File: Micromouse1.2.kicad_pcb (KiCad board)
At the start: 2 copper layers, 70.4 x 87.9 mm, 132 parts, among them J1 USB_B, P1 CONN_01X4, Q1 Q_NMOS_DGS, Q2 Q_NMOS_DGS, Q3 Q_NMOS_DGS, Q4 Q_NMOS_DGS, Q5 Q_NMOS_DGS, Q6 Q_NMOS_DGS, U1 BAT54C, U10 CONN_02X03, U14 600, U15 LMZ21701, U16 JST_Connector, U17 Switch_micromouse, U18 LMZ21701, U19 splitter, U2 DRV8833, U20 TPD3S014, U21 MKL02Z32VFG4, U22 LP38691, U23 MK66FX1M0, U24 Test_Point, U25 Test_Point, U26 Test_Point, U27 Test_Point, U28 Test_Point, U29 Test_Point, U3 120, U30 Test_Point, U31 MPU-6500, U32 Motor_mount, U4 TPS61222DCK, U5 600, U6 BAT54C, U7 Test_Point, U9 CONN_02X03, Y1 Crystal_16MHz, Y2 32.768MHz

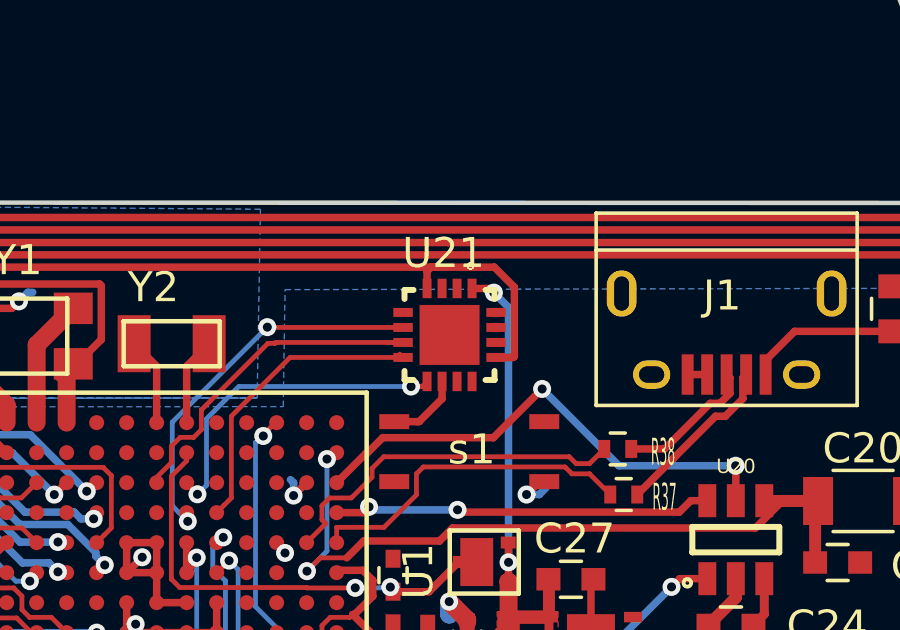
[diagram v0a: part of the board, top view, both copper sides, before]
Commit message: fixed the unconnected teensy bootloader chip
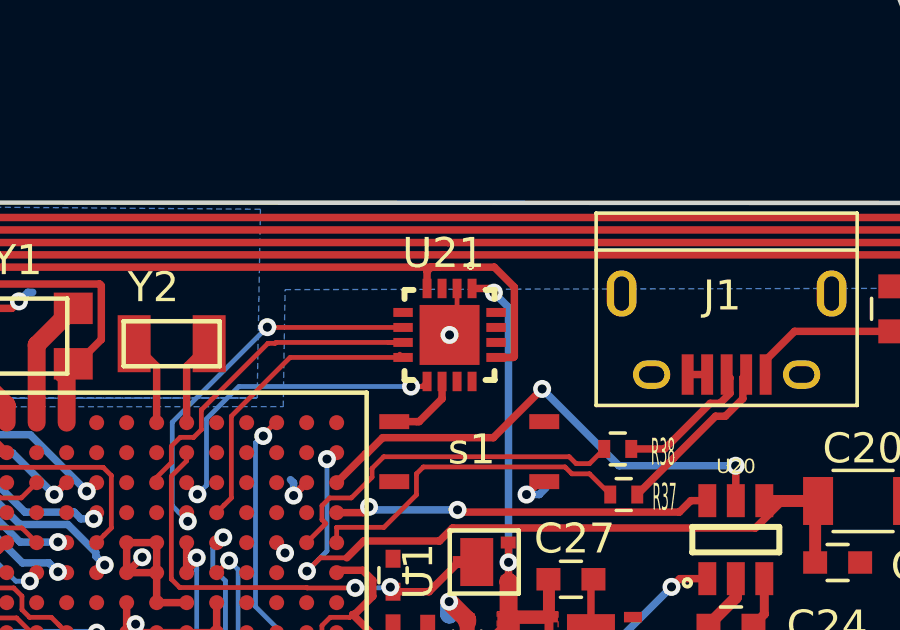
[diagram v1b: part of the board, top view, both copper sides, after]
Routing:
- net GNDD: track 81.4 -> 83.1 mm, vias 15 -> 16
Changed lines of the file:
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@@
 (kicad_pcb (version 4) (host pcbnew 4.0.6)
   (general
-    (links 301)
-    (no_connects 16)
-    (area 79.0524 22.0566 163.872401 130.206601)
+    (links 302)
+    (no_connects 17)
+    (area 83.557399 26.541599 153.967401 114.471601)
     (thickness 1.6)
     (drawings 18)
-    (tracks 1187)
+    (tracks 1190)
     (zones 0)
     (modules 132)
@@
   (page A4)
   (layers
-    (0 F.Cu signal)
+    (0 F.Cu signal hide)
     (31 B.Cu signal)
     (32 B.Adhes user)
@@
   )
   (setup
-    (last_trace_width 0.25)
+    (last_trace_width 0.16)
     (user_trace_width 0.15)
     (user_trace_width 0.16)
@@
     (mod_text_size 1 1)
     (mod_text_width 0.15)
-    (pad_size 0.5 0.5)
+    (pad_size 2 2)
     (pad_drill 0)
     (pad_to_mask_clearance 0.2)
     (aux_axis_origin 0 0)
     (grid_origin 150.0124 -13.2334)
-    (visible_elements 7FFFFFFF)
+    (visible_elements 7FFFFDFF)
     (pcbplotparams
       (layerselection 0x010f0_80000001)
@@
     (pad 16 smd rect (at -0.75 -1.55 180) (size 0.65 0.3) (layers F.Cu F.Paste F.Mask)
       (net 70 "Net-(U21-Pad16)"))
-    (pad 17 smd rect (at 0 0 270) (size 2 2) (layers F.Cu F.Paste F.Mask))
+    (pad PAD smd rect (at 0 0 270) (size 2 2) (layers F.Cu F.Paste F.Mask)
+      (net 5 GNDD))
   )
   (module micromouse:32.768_CRYSTAL (layer F.Cu)
@@
   (segment (start 85.396166 54.420366) (end 85.3824 54.4066) (width 0.6) (layer F.Cu) (net 3))
   (via (at 85.3824 54.4066) (size 0.6) (drill 0.3) (layers F.Cu B.Cu) (net 3))
+  (segment (start 122.086 61.807) (end 122.086 63.107) (width 0.16) (layer F.Cu) (net 5))
+  (segment (start 122.086 63.107) (end 121.836 63.357) (width 0.16) (layer F.Cu) (net 5))
+  (via (at 121.836 63.357) (size 0.6) (drill 0.3) (layers F.Cu B.Cu) (net 5))
   (segment (start 107.4824 62.2366) (end 107.782399 61.936601) (width 0.25) (layer B.Cu) (net 5))
   (segment (start 107.782399 61.936601) (end 107.942399 61.936601) (width 0.25) (layer B.Cu) (net 5))
